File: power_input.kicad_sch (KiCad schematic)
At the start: 18 parts, among them J2 Barrel_Jack_Switch, Q4 AO4805, U3 DZDH0401DW, U4 INA180A4, U5 DZDH0401DW

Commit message: WIP PCb routing
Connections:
- net VCCQ: now also Q4.7 (D), Q4.8 (G); no longer Q4.5 (D), Q4.6 (G)
- net VIN: now also Q4.5 (D), Q4.6 (G); no longer Q4.7 (D), Q4.8 (G)
- net at R27.1, U5.3 (BIAS): now also Q4.2 (G); no longer Q4.4 (G)
- net PWRIN: now reaches R19.1, R20.1, R22.1, U3.4 (SOURCE), U5.4 (SOURCE)
- net PWRIN: now also Q4.1 (S), Q4.3 (S); no longer Q4.1 (S), Q4.3 (S)
- net at R25.1, U3.3 (BIAS): now also Q4.4 (G); no longer Q4.2 (G)
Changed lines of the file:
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@@
+    (effects (font (size 1.27 1.27)) (justify left bottom))
+  )
+  (label "PWRIN" (at 133.35 31.75 0)
     (effects (font (size 1.27 1.27)) (justify left bottom))
   )
@@
     (pin "2")
   )
-  (symbol (lib_id "Device:Q_Dual_PMOS_S1G1S2G2D2D2D1D1") (at 88.9 95.25 90) (unit 2)
+  (symbol (lib_id "Device:Q_Dual_PMOS_S1G1S2G2D2D2D1D1") (at 88.9 95.25 90) (unit 1)
     (in_bom yes) (on_board yes) (fields_autoplaced)
     (property "Reference" "Q4" (id 0) (at 88.9 85.09 90))
@@
     (pin "1")
   )
-  (symbol (lib_id "Device:Q_Dual_PMOS_S1G1S2G2D2D2D1D1") (at 88.9 34.29 90) (unit 1)
+  (symbol (lib_id "Device:Q_Dual_PMOS_S1G1S2G2D2D2D1D1") (at 88.9 34.29 90) (unit 2)
     (in_bom yes) (on_board yes) (fields_autoplaced)
     (property "Reference" "Q4" (id 0) (at 88.9 24.13 90))

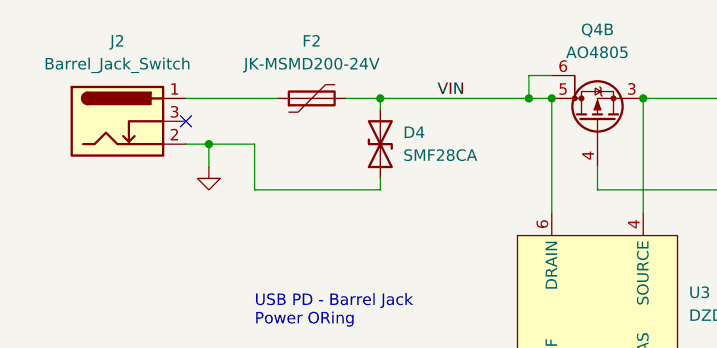
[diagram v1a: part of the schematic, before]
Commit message: Add information and BOM consolidation for JLCPCB
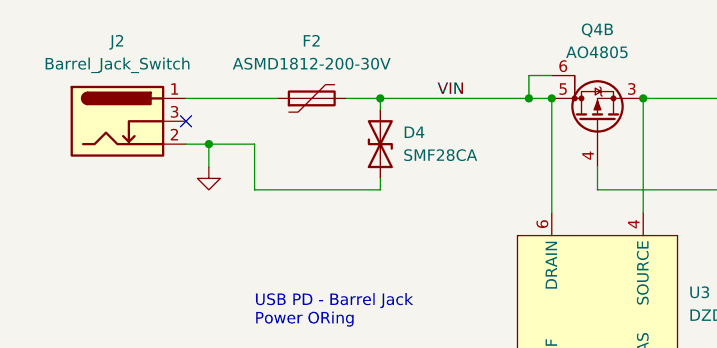
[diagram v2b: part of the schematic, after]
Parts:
- F2: value JK-MSMD200-24V -> ASMD1812-200-30V
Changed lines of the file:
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@@
     (in_bom yes) (on_board yes) (fields_autoplaced)
     (property "Reference" "F2" (id 0) (at 57.15 25.4 90))
-    (property "Value" "JK-MSMD200-24V" (id 1) (at 57.15 27.94 90))
+    (property "Value" "ASMD1812-200-30V" (id 1) (at 57.15 27.94 90))
     (property "Footprint" "Fuse:Fuse_1812_4532Metric" (id 2) (at 62.23 30.48 0)
       (effects (font (size 1.27 1.27)) (justify left) hide)

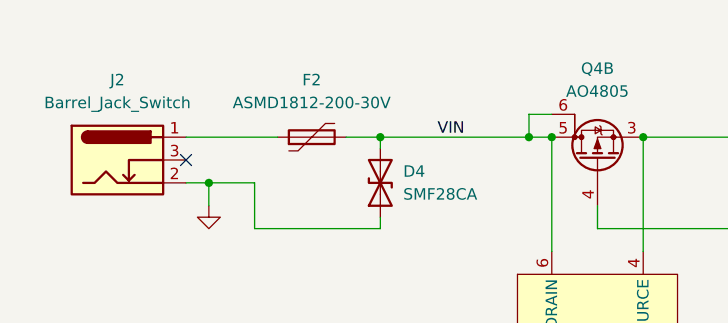
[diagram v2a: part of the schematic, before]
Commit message: Power optimization, add Aisler Assembly MPN info
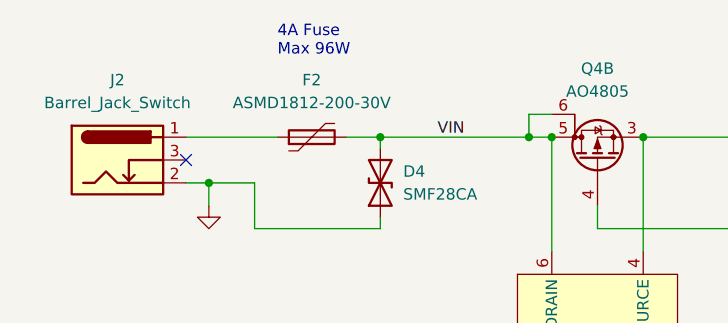
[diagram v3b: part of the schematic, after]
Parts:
- C7: MPN (none) -> 100nF 50V X7R
- D4: MPN (none) -> SMF28CA
- F2: MPN (none) -> ASMD1812-200-30V
- J2: MPN (none) -> DC-005-5A-2.0
- Q4: MPN (none) -> AO4805
- R19: MPN (none) -> 1m5R 1%
- R20, R24, R26: MPN (none) -> 100K 1%
- R21: MPN (none) -> 5K1 1%
- R22, R23: MPN (none) -> 0R 1%
- R25, R27: MPN (none) -> 1M 1%
- U3, U5: MPN (none) -> DZDH0401DW-7
- U4: MPN (none) -> INA180A4IDBVR
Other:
- note added: "4A Fuse Max 96W"
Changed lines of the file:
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@@
     (stroke (width 0) (type default) (color 0 0 0 0))
+  )
+  (text "4A Fuse\nMax 96W" (at 53.34 22.86 0)
+    (effects (font (size 1.27 1.27)) (justify left bottom))
   )
   (text "STM32 Vrefint = 1.23V\nVsense(max) = 25.348V" (at 142.24 48.26 0)
@@
       (effects (font (size 1.27 1.27)) hide)
     )
+    (property "MPN" "1M 1%" (id 4) (at 93.98 132.08 0)
+      (effects (font (size 1.27 1.27)) hide)
+    )
     (pin "1")
     (pin "2")
@@
     )
     (property "Datasheet" "~" (id 3) (at 88.9 93.98 0)
+      (effects (font (size 1.27 1.27)) hide)
+    )
+    (property "MPN" "AO4805" (id 4) (at 88.9 34.29 0)
       (effects (font (size 1.27 1.27)) hide)
     )
@@
       (effects (font (size 1.27 1.27)) hide)
     )
+    (property "MPN" "DC-005-5A-2.0" (id 4) (at 35.56 34.29 0)
+      (effects (font (size 1.27 1.27)) hide)
+    )
     (pin "1")
     (pin "2")
@@
       (effects (font (size 1.27 1.27)) hide)
     )
+    (property "MPN" "INA180A4IDBVR" (id 4) (at 238.76 54.61 0)
+      (effects (font (size 1.27 1.27)) hide)
+    )
     (pin "1")
     (pin "2")
@@
     )
     (property "Datasheet" "~" (id 3) (at 88.9 33.02 0)
+      (effects (font (size 1.27 1.27)) hide)
+    )
+    (property "MPN" "AO4805" (id 4) (at 88.9 34.29 0)
       (effects (font (size 1.27 1.27)) hide)
     )
@@
       (effects (font (size 1.27 1.27)) hide)
     )
+    (property "MPN" "1M 1%" (id 4) (at 93.98 71.12 0)
+      (effects (font (size 1.27 1.27)) hide)
+    )
     (pin "1")
     (pin "2")
@@
       (effects (font (size 1.27 1.27)) hide)
     )
+    (property "MPN" "0R 1%" (id 4) (at 212.09 52.07 0)
+      (effects (font (size 1.27 1.27)) hide)
+    )
     (pin "1")
     (pin "2")
@@
       (effects (font (size 1.27 1.27)) hide)
     )
+    (property "MPN" "100K 1%" (id 4) (at 83.82 132.08 0)
+      (effects (font (size 1.27 1.27)) hide)
+    )
     (pin "1")
     (pin "2")
@@
     )
     (property "Datasheet" "https://www.diodes.com/assets/Datasheets/DZDH0401DW.pdf" (id 3) (at 130.81 124.46 0)
+      (effects (font (size 1.27 1.27)) hide)
+    )
+    (property "MPN" "DZDH0401DW-7" (id 4) (at 88.9 115.57 0)
       (effects (font (size 1.27 1.27)) hide)
     )
@@
     )
     (property "Datasheet" "~" (id 3) (at 168.91 41.91 0)
+      (effects (font (size 1.27 1.27)) hide)
+    )
+    (property "MPN" "100K 1%" (id 4) (at 168.91 41.91 0)
       (effects (font (size 1.27 1.27)) hide)
     )
@@
       (effects (font (size 1.27 1.27)) hide)
     )
+    (property "MPN" "0R 1%" (id 4) (at 212.09 57.15 0)
+      (effects (font (size 1.27 1.27)) hide)
+    )
     (pin "1")
     (pin "2")
@@
       (effects (font (size 1.27 1.27)) hide)
     )
+    (property "MPN" "1m5R 1%" (id 4) (at 201.93 31.75 0)
+      (effects (font (size 1.27 1.27)) hide)
+    )
     (pin "1")
     (pin "2")
@@
     )
     (property "Datasheet" "https://www.diodes.com/assets/Datasheets/DZDH0401DW.pdf" (id 3) (at 130.81 63.5 0)
+      (effects (font (size 1.27 1.27)) hide)
+    )
+    (property "MPN" "DZDH0401DW-7" (id 4) (at 88.9 54.61 0)
       (effects (font (size 1.27 1.27)) hide)
     )
@@
       (effects (font (size 1.27 1.27)) hide)
     )
+    (property "MPN" "5K1 1%" (id 4) (at 168.91 52.07 0)
+      (effects (font (size 1.27 1.27)) hide)
+    )
     (pin "1")
     (pin "2")
@@
     )
     (property "Datasheet" "~" (id 3) (at 245.11 43.18 0)
+      (effects (font (size 1.27 1.27)) hide)
+    )
+    (property "MPN" "100nF 50V X7R" (id 4) (at 245.11 43.18 0)
       (effects (font (size 1.27 1.27)) hide)
     )
@@
       (effects (font (size 1.27 1.27)) hide)
     )
+    (property "MPN" "SMF28CA" (id 4) (at 64.77 36.83 0)
+      (effects (font (size 1.27 1.27)) hide)
+    )
     (pin "1")
     (pin "2")
@@
     )
     (property "Datasheet" "~" (id 3) (at 83.82 71.12 0)
+      (effects (font (size 1.27 1.27)) hide)
+    )
+    (property "MPN" "100K 1%" (id 4) (at 83.82 71.12 0)
       (effects (font (size 1.27 1.27)) hide)
     )
@@
       (effects (font (size 1.27 1.27)) hide)
     )
+    (property "MPN" "ASMD1812-200-30V" (id 4) (at 57.15 31.75 0)
+      (effects (font (size 1.27 1.27)) hide)
+    )

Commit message: Create IBOM, Add sheet info
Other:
- company: (none) -> Sleepy Pony Labs
- title: (none) -> Dual Rail Breadboard Power Supply
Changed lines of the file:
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@@
 (kicad_sch (version 20211123) (generator eeschema)
   (paper "A4")
+  (title_block
+    (title "Dual Rail Breadboard Power Supply")
+    (date "2023-06-11")
+    (rev "1")
+    (company "Sleepy Pony Labs")
+  )
   (junction (at 168.91 46.99) (diameter 0) (color 0 0 0 0)
   )
